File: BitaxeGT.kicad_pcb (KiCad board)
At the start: 6 copper layers, 65 x 112 mm, 194 parts, among them J1 XT30, J2 Conn_01x08, J3 Conn_01x04, J4 USB_C_Receptacle_USB2.0, J7 Conn_01x04, J8 TC2030-IDC, SW1 SWITCH-SPST, SW2 SWITCH-SPST, U1 TPS546D24ARVFR, U10 BM1370_mode1, U11 MCP1824T-1202E/OT, U12 MCP1824T-0802E, U13 EMC2103-2, U2 SN74AVC4T774, U3 TPSM861253RDXR, U4 TPS546D24ARVFR, U5 L78L05_SOT89, U6 ESP32-S3-WROOM-1, U8 25MHz, U9 BM1370_mode1

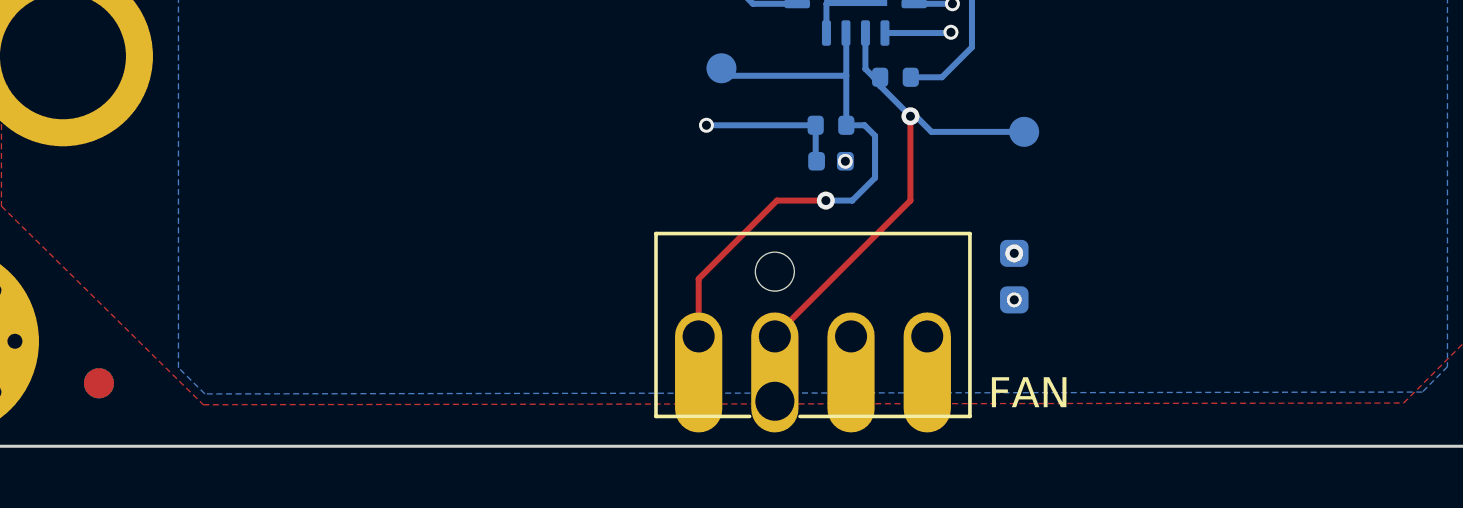
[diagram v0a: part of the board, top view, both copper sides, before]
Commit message: add TCH logo
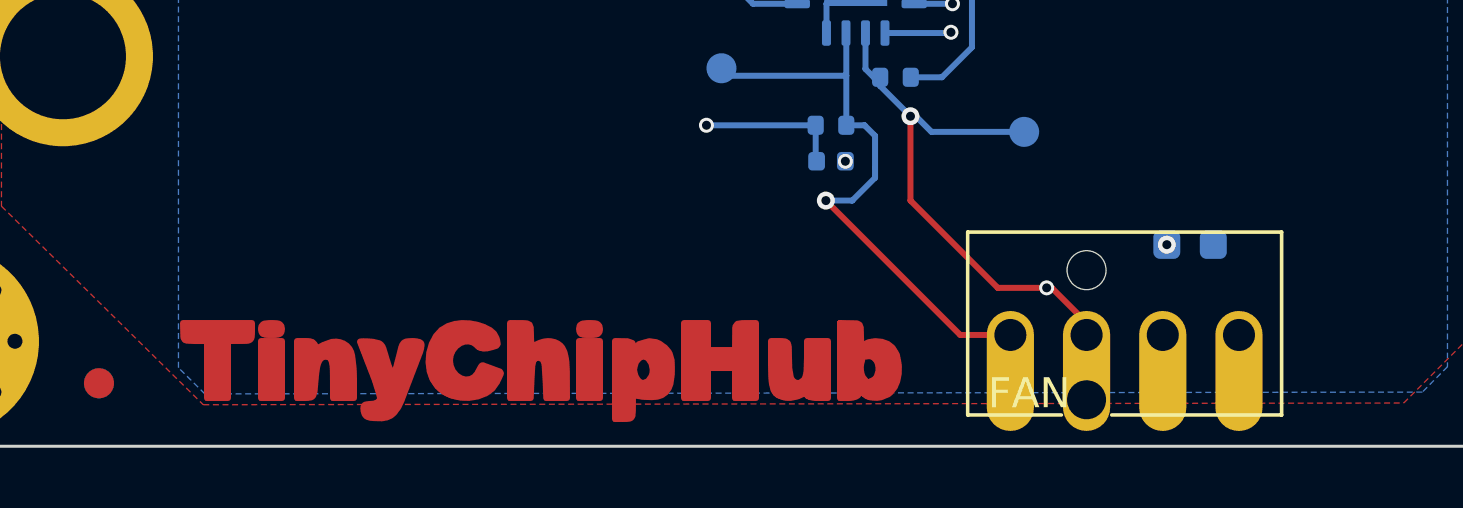
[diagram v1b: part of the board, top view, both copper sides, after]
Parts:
- added LG1: ~, TinyChipHub:TCH-Logo, F.Cu at (121.3, 147.6)
- added LG2: ~, TinyChipHub:TCH-Logo-Mask, F.Cu at (121.3, 148.2)
- moved J7 10.4 mm to (141.4, 146.3)
- moved C41 5.96 mm to (143.6, 143.3), turned to 0 degrees
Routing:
- net /12V: track 104.5 -> 95.7 mm
- net /fan/FAN_TACH: track 16.8 -> 18.4 mm, vias 1 -> 2
- net /fan/FAN_PWM: track 19.0 -> 19.8 mm
- net GND: vias 332 -> 331

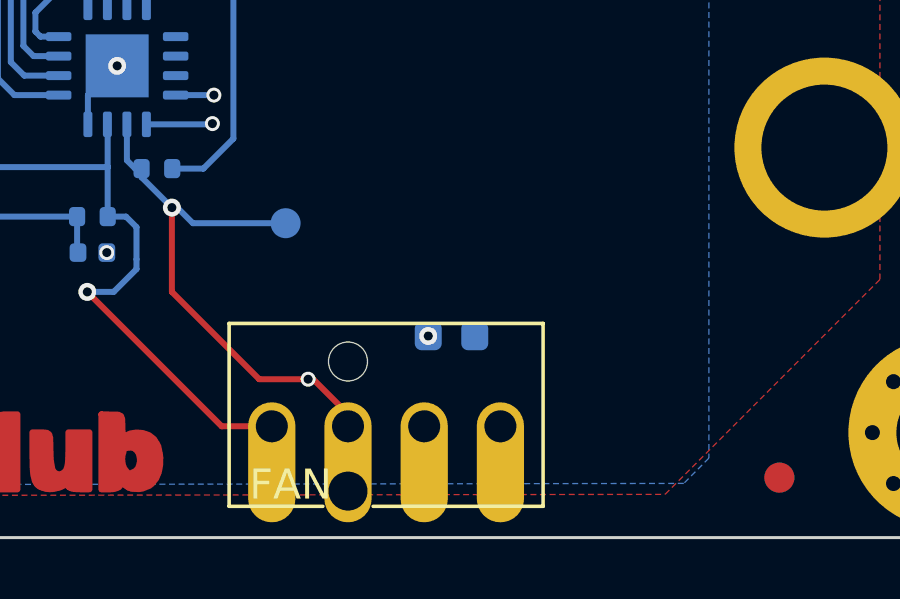
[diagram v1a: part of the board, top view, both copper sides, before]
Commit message: Start changing ldo to match our production
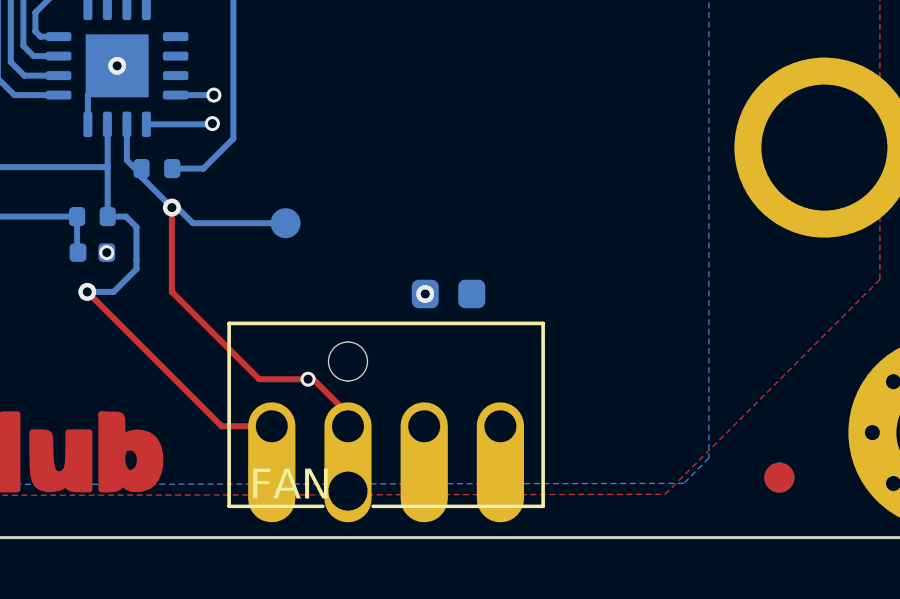
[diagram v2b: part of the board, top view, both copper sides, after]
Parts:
- moved C41 1.40 mm to (143.5, 141.9)
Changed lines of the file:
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@@
 	(footprint "Capacitor_SMD:C_0603_1608Metric"
 		(layer "B.Cu")
-		(at 143.57 143.28)
+		(at 143.47 141.88)
 		(descr "Capacitor SMD 0603 (1608 Metric), square (rectangular) end terminal, IPC_7351 nominal, (Body size source: IPC-SM-782 page 76, https://www.pcb-3d.com/wordpress/wp-content/uploads/ipc-sm-782a_amendment_1_and_2.pdf), generated with kicad-footprint-generator")
 		(tags "capacitor")
@@
 	)
 	(via
-		(at 142.795 143.28)
+		(at 142.695 141.88)
 		(size 0.6)
 		(drill 0.3)

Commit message: final update
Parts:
- removed C39, C43, C44: 10uF, Capacitor_SMD:C_0603_1608Metric
- removed C46, C47: 1uF, Capacitor_SMD:C_0402_1005Metric
- removed R17: 20k, Resistor_SMD:R_0402_1005Metric
- removed R18: 10k, Resistor_SMD:R_0402_1005Metric
- removed TP27: 5V, TestPoint:TestPoint_Pad_D1.5mm
- removed TP28: GND, TestPoint:TestPoint_Pad_D1.5mm
- removed U3: TPSM861253RDXR, bitaxe:TPSM863257RDX
- added C100: 1uF, Capacitor_SMD:C_0402_1005Metric, B.Cu at (140.7, 56.3)
- added C101: 1uF, Capacitor_SMD:C_0402_1005Metric, B.Cu at (142.2, 52.4)
- added C50: 10uF, Capacitor_SMD:C_0805_2012Metric, B.Cu at (137.1, 68.3)
- added C63: 10uF, Capacitor_SMD:C_0805_2012Metric, B.Cu at (137.1, 70.4)
- added C96: 100nF, Capacitor_SMD:C_0603_1608Metric, B.Cu at (136.9, 66.4)
- added C97: 0.1uF, Capacitor_SMD:C_0402_1005Metric, B.Cu at (133.8, 66.3)
- added C98: 10uF, Capacitor_SMD:C_0805_2012Metric, B.Cu at (131.1, 59.2)
- added C99: 10uF, Capacitor_SMD:C_0805_2012Metric, B.Cu at (131.1, 57.2)
- added L3: 8.2 uH, Zyber:74438357082, B.Cu at (133.3, 62.7)
- added R41: 30k, Resistor_SMD:R_0402_1005Metric, B.Cu at (136.9, 60.3)
- added R42: 5.1k, Resistor_SMD:R_0402_1005Metric, B.Cu at (136.9, 59.2)
- added U7: LMR54410, Package_TO_SOT_SMD:SOT-23-6, B.Cu at (137.6, 63.0)
- L1, L2: value 300nH -> 220nH
- U11: value MCP1824T-1202E/OT -> RT9080-12GJ5
- U12: value MCP1824T-0802E -> RT9080-08GJ5-MS
- U2: value SN74AVC4T774 -> SN74AXC4T774BQBR
- U5: value L78L05_SOT89 -> RT9080-33GJ5; footprint Package_TO_SOT_SMD:SOT-89-3 -> Zyber:RT9080-33GJ5
- moved U5 8.33 mm to (139.2, 53.8), turned to 90 degrees
- moved H1 2.50 mm to (162.5, 41.5)
- moved H2 2.50 mm to (99.5, 41.5)
- moved H3 2.50 mm to (162.5, 146.5)
- moved H4 2.50 mm to (99.5, 146.5)
- moved LG2 0.07 mm to (121.3, 148.2)
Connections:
- U5 pad 3: /12V -> /5V
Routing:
- net GND: track 98.4 -> 122.6 mm, vias 331 -> 309
- net /3V3: track 145.5 -> 151.9 mm, vias 13 -> 12
- net Net-(U7-CB): track 0.00 -> 5.48 mm, vias 0 -> 2
- net /5V: track 184.2 -> 189.1 mm, vias 9 -> 8
- net Net-(U3-EN): track 3.46 -> 0.00 mm
- net Net-(U7-FB): track 0.00 -> 3.10 mm
- net /12V: track 95.7 -> 93.3 mm
- net Net-(U7-SW): track 0.00 -> 2.01 mm
- added copper zone on B.Cu, net Net-(U7-SW)
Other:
- board size 65 x 112 mm -> 70 x 112 mm

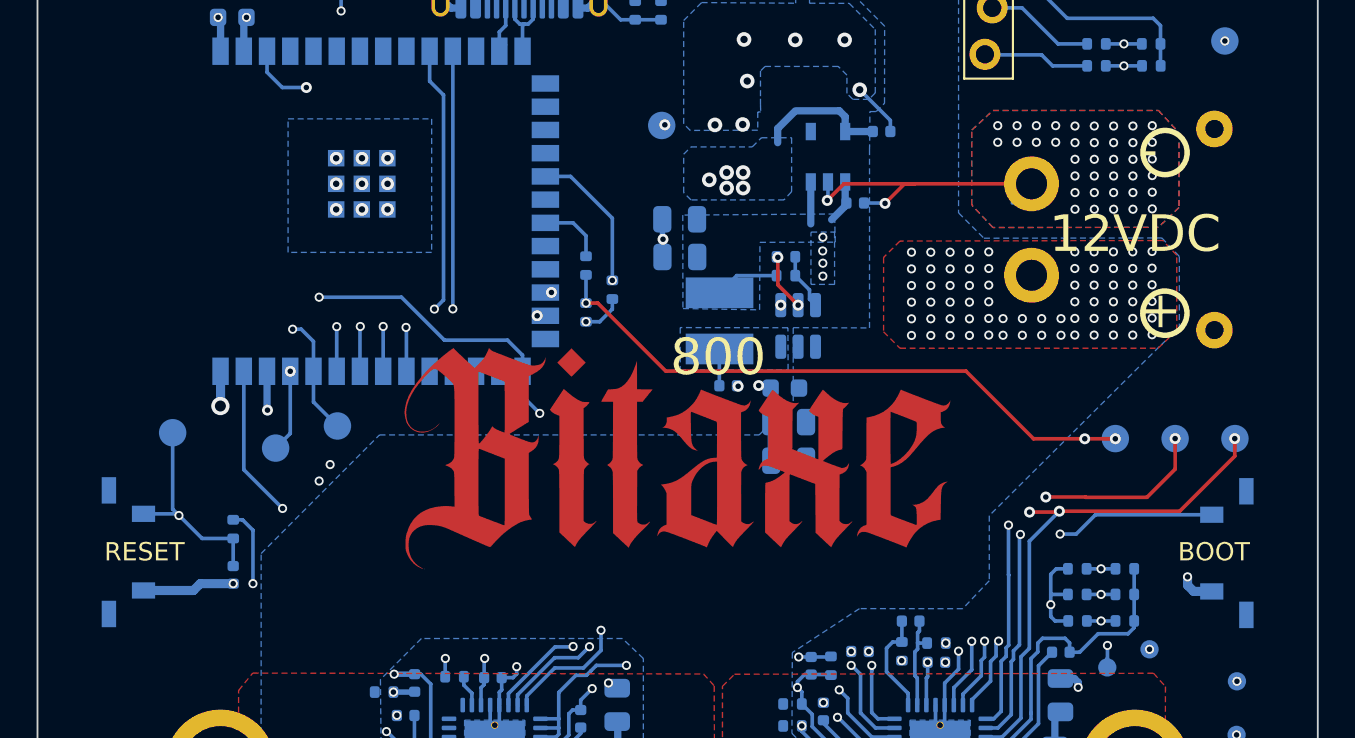
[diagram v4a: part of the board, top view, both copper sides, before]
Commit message: tune component positions
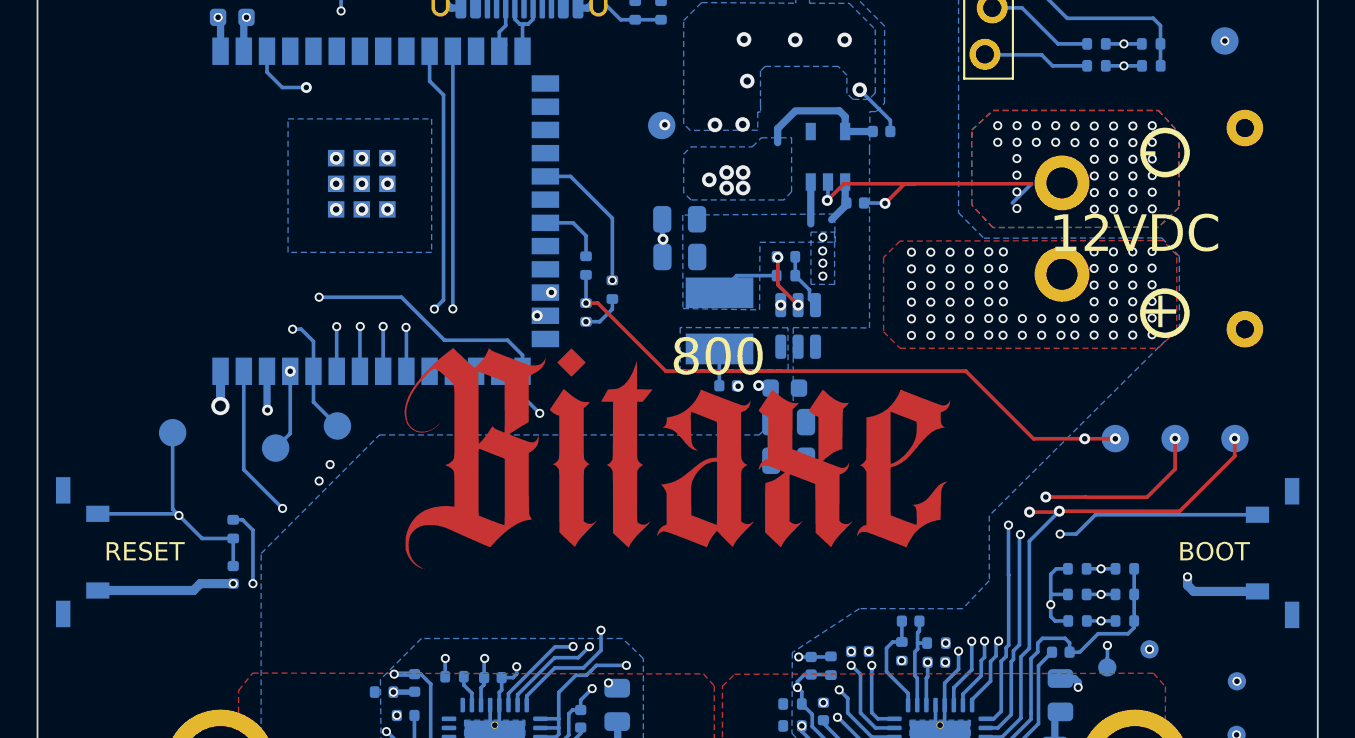
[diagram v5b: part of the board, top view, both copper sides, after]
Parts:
- moved SW1 2.50 mm to (97.9, 75.4)
- moved SW2 2.50 mm to (164.1, 75.4)
- moved J1 1.67 mm to (152.0, 57.7)
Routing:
- net GND: track 122.6 -> 127.6 mm
- net /ESP32/IO0: track 91.2 -> 93.7 mm
- net /ESP32/EN: track 50.1 -> 52.6 mm
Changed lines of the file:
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@@
 		(tags "test point SMD pad")
 		(property "Reference" "TP25"
-			(at -1.44 -2.76 90)
+			(at -2.21 -0.19 90)
 			(layer "B.SilkS")
 			(effects
@@
 	(footprint "bitaxe:SW_TL3330AF130QG_EWI"
 		(layer "B.Cu")
-		(at 100.4 75.39 90)
+		(at 97.9 75.39 90)
 		(tags "TL3330AF130QG ")
 		(property "Reference" "SW1"
@@
 	(footprint "bitaxe:XT30PW-M"
 		(layer "B.Cu")
-		(at 150.35 57.75 90)
+		(at 152.015 57.7 90)
 		(property "Reference" "J1"
 			(at 0.15 -1.5 0)
@@
 	(footprint "bitaxe:SW_TL3330AF130QG_EWI"
 		(layer "B.Cu")
-		(at 161.6 75.44 -90)
+		(at 164.1 75.44 -90)
 		(tags "TL3330AF130QG ")
 		(property "Reference" "SW2"
@@
 	)
 	(gr_circle
-		(center 146.84 55.27)
-		(end 147.81 54.55)
+		(center 147.84 55.27)
+		(end 148.81 54.55)
 		(stroke
 			(width 0.3)
@@
 	)
 	(gr_circle
-		(center 146.88 60.28)
-		(end 147.85 59.56)
+		(center 147.88 60.28)
+		(end 148.85 59.56)
 		(stroke
 			(width 0.3)
@@
 	)
 	(gr_text "+"
-		(at 145.49 59.2665 180)
+		(at 146.49 59.2665 180)
 		(layer "B.SilkS")
 		(effects
@@
 	)
 	(gr_text "-"
-		(at 145.458015 54.23 180)
+		(at 146.458015 54.23 180)
 		(layer "B.SilkS")
 		(effects
@@
 	)
 	(via
-		(at 152.715 61.7)
+		(at 148.81 61.7)
 		(size 0.5)
 		(drill 0.3)
@@
 	)
 	(via
-		(at 152.715 58.97)
+		(at 148.81 58.97)
 		(size 0.5)
 		(drill 0.3)
@@
 	)
 	(via
-		(at 152.715 60.79)
+		(at 148.81 60.79)
 		(size 0.5)
 		(drill 0.3)
@@
 	)
 	(via
-		(at 152.715 59.88)
+		(at 148.81 59.88)
 		(size 0.5)
 		(drill 0.3)
@@
 	)
 	(via
-		(at 152.725 56.64)
+		(at 149.55 56.6)
 		(size 0.5)
 		(drill 0.3)
@@
 	)
 	(via
-		(at 152.725 55.73)
+		(at 149.55 55.69)
 		(size 0.5)
 		(drill 0.3)
@@
 	)
 	(via
-		(at 152.725 54.82)
+		(at 149.55 54.78)
 		(size 0.5)
 		(drill 0.3)
@@
 	)
 	(via
-		(at 152.725 53.91)
+		(at 149.55 53.87)
 		(size 0.5)
 		(drill 0.3)
@@
 	)
 	(segment
-		(start 160.203 77.5355)
-		(end 159.2155 77.5355)
+		(start 159.2155 77.5355)
+		(end 158.88 77.2)
 		(width 0.5)
 		(layer "B.Cu")
@@
 	)
 	(segment
-		(start 104.901 77.11)
-		(end 104.5255 77.4855)
-		(width 0.5)
-		(layer "B.Cu")
-		(net 120)
-	)
-	(segment
 		(start 124.45 119.95)
 		(end 124.45 119.3)
@@
 	)
 	(segment
-		(start 104.5255 77.4855)
-		(end 101.797 77.4855)
-		(width 0.5)
-		(layer "B.Cu")
-		(net 120)
-	)
-	(segment
 		(start 127.25 82.8)
 		(end 127.4375 82.8)
@@
 	)
 	(segment
-		(start 106.7 77.11)
-		(end 104.901 77.11)
-		(width 0.5)
-		(layer "B.Cu")
-		(net 120)
-	)
-	(segment
 		(start 106.070001 122.329999)
 		(end 106.9 121.5)
@@
 	)
 	(segment
+		(start 104.901 77.11)
+		(end 104.5255 77.4855)
+		(width 0.5)
+		(layer "B.Cu")
+		(net 120)
+	)
+	(segment
+		(start 104.5255 77.4855)
+		(end 99.297 77.4855)
+		(width 0.5)
+		(layer "B.Cu")
+		(net 120)
+	)
+	(segment
 		(start 103.7 99.5)
 		(end 104.4 100.2)
@@
 	)
 	(segment
-		(start 145.1 83.75)
-		(end 145.1 87)
-		(width 0.2)
+		(start 158.88 77.2)
+		(end 158.88 76.74)
+		(width 0.5)
 		(layer "B.Cu")
 		(net 120)
 	)
 	(segment
-		(start 159.2155 77.5355)
-		(end 158.88 77.2)
-		(width 0.5)
+		(start 145.1 83.75)
+		(end 145.1 87)
+		(width 0.2)
 		(layer "B.Cu")
 		(net 120)
@@
 	)
 	(segment
+		(start 106.7 77.11)
+		(end 104.901 77.11)
+		(width 0.5)
+		(layer "B.Cu")
+		(net 120)
+	)
+	(segment
 		(start 128.68 46.28)
 		(end 127.885 46.28)
@@
 	)
 	(segment
-		(start 158.88 77.2)
-		(end 158.88 76.74)
-		(width 0.5)
-		(layer "B.Cu")
-		(net 120)
-	)
-	(segment
 		(start 152.6875 82.2975)
 		(end 151.93 82.2975)
@@
 	)
 	(segment
+		(start 162.703 77.5355)
+		(end 159.2155 77.5355)
+		(width 0.5)
+		(layer "B.Cu")
+		(net 120)
+	)
+	(segment
 		(start 149.3 56.3)
 		(end 150.35 55.25)
@@
 	)
 	(segment
-		(start 105 74.64)
-		(end 106.7 74.64)
+		(start 106.7 74.64)
+		(end 105 74.64)
 		(width 0.2)
 		(layer "B.Cu")
@@
 	)
 	(segment
-		(start 103.6545 73.2945)
-		(end 105 74.64)
-		(width 0.2)
-		(layer "B.Cu")
-		(net 130)
-	)
-	(segment
 		(start 114.67 44.2)
 		(end 114.67 43.1)
@@
 	)
 	(segment
-		(start 101.797 73.2945)
+		(start 105 74.64)
 		(end 103.6545 73.2945)
 		(width 0.2)
@@
 	)
 	(segment
+		(start 103.6545 73.2945)
+		(end 99.297 73.2945)
+		(width 0.2)
+		(layer "B.Cu")
+		(net 130)
+	)
+	(segment
 		(start 114.67 44.2)
 		(end 114.67 46.014314)
@@
 	)
 	(segment
-		(start 152.79 74.4)
-		(end 153.8455 73.3445)
+		(start 122.52 65.5)
+		(end 122.52 66.86)
 		(width 0.2)
 		(layer "B.Cu")
@@
 	)
 	(segment
-		(start 122.52 65.5)
-		(end 122.52 66.86)
+		(start 151.91 74.4)
+		(end 152.79 74.4)
 		(width 0.2)
 		(layer "B.Cu")
@@
 	(segment
 		(start 153.8455 73.3445)
-		(end 160.203 73.3445)
+		(end 162.703 73.3445)
 		(width 0.2)
 		(layer "B.Cu")
@@
 	)
 	(segment
-		(start 151.91 74.4)
-		(end 152.79 74.4)
+		(start 122.52 64.62)
+		(end 122.52 65.5)
 		(width 0.2)
 		(layer "B.Cu")
@@
 	)
 	(segment
-		(start 122.52 64.62)
-		(end 122.52 65.5)
+		(start 152.79 74.4)
+		(end 153.8455 73.3445)
 		(width 0.2)
 		(layer "B.Cu")
